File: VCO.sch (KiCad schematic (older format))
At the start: 76 parts, among them J1 Conn_01x05_Male, J10 FM, J12 PW, J13 saw, J14 sq, J3 V/oct, J4 Conn_01x05_Male, J5 Conn_01x05_Male, J6 Conn_01x05_Male, J8 Conn_01x05_Male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

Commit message: Edeting .gitignore
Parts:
- C10, C7, C8, C9: value 1u -> C
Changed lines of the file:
@@
 $EndComp
 $Comp
-L uRack:-9V #PWR0105
+L power:-9V #PWR0105
 U 1 1 5FD658D4
 P 1550 6500
@@
 $EndComp
 $Comp
-L uRack:+9V #PWR0106
+L power:+9V #PWR0106
 U 1 1 5FD84C6F
 P 1650 5200
@@
 P 2950 5500
 F 0 "C9" H 3065 5546 50  0000 L CNN
-F 1 "1u" H 3065 5455 50  0000 L CNN
+F 1 "C" H 3065 5455 50  0000 L CNN
 F 2 "Capacitor_SMD:C_0603_1608Metric_Pad1.05x0.95mm_HandSolder" H 2988 5350 50  0001 C CNN
 F 3 "~" H 2950 5500 50  0001 C CNN
@@
 P 2950 6200
 F 0 "C10" H 3065 6246 50  0000 L CNN
-F 1 "1u" H 3065 6155 50  0000 L CNN
+F 1 "C" H 3065 6155 50  0000 L CNN
 F 2 "Capacitor_SMD:C_0603_1608Metric_Pad1.05x0.95mm_HandSolder" H 2988 6050 50  0001 C CNN
 F 3 "~" H 2950 6200 50  0001 C CNN
@@
 P 1750 5550
 F 0 "C7" H 1865 5596 50  0000 L CNN
-F 1 "1u" H 1865 5505 50  0000 L CNN
+F 1 "C" H 1865 5505 50  0000 L CNN
 F 2 "Capacitor_SMD:C_0603_1608Metric_Pad1.05x0.95mm_HandSolder" H 1788 5400 50  0001 C CNN
 F 3 "~" H 1750 5550 50  0001 C CNN
@@
 P 1750 6150
 F 0 "C8" H 1865 6196 50  0000 L CNN
-F 1 "1u" H 1865 6105 50  0000 L CNN
+F 1 "C" H 1865 6105 50  0000 L CNN
 F 2 "Capacitor_SMD:C_0603_1608Metric_Pad1.05x0.95mm_HandSolder" H 1788 6000 50  0001 C CNN
 F 3 "~" H 1750 6150 50  0001 C CNN
@@
 $EndComp
 $Comp
-L uRack:GNDREF #PWR0109
+L uRack:GNDREF #PWR?
 U 1 1 5FA50368
 P 2200 2000
-F 0 "#PWR0109" H 2200 1750 50  0001 C CNN
+F 0 "#PWR?" H 2200 1750 50  0001 C CNN
 F 1 "GNDREF" H 2205 1827 50  0000 C CNN
 F 2 "" H 2200 2000 50  0001 C CNN
@@
 $EndComp
 $Comp
-L uRack:GNDREF #PWR0110
+L uRack:GNDREF #PWR?
 U 1 1 5FA5270D
 P 2500 2000
-F 0 "#PWR0110" H 2500 1750 50  0001 C CNN
+F 0 "#PWR?" H 2500 1750 50  0001 C CNN
 F 1 "GNDREF" H 2505 1827 50  0000 C CNN
 F 2 "" H 2500 2000 50  0001 C CNN
@@
 $EndComp
 $Comp
-L uRack:GNDREF #PWR0111
+L uRack:GNDREF #PWR?
 U 1 1 5FA67393
 P 2800 2000
-F 0 "#PWR0111" H 2800 1750 50  0001 C CNN
+F 0 "#PWR?" H 2800 1750 50  0001 C CNN
 F 1 "GNDREF" H 2805 1827 50  0000 C CNN
 F 2 "" H 2800 2000 50  0001 C CNN
@@
 $EndComp
 $Comp
-L uRack:GNDREF #PWR0112
+L uRack:GNDREF #PWR?
 U 1 1 5FA7CC97
 P 3700 1850
-F 0 "#PWR0112" H 3700 1600 50  0001 C CNN
+F 0 "#PWR?" H 3700 1600 50  0001 C CNN
 F 1 "GNDREF" H 3705 1677 50  0000 C CNN
 F 2 "" H 3700 1850 50  0001 C CNN
@@
 $EndComp
 $Comp
-L uRack:GNDREF #PWR0113
+L uRack:GNDREF #PWR?
 U 1 1 5FA921D0
 P 4850 3300
-F 0 "#PWR0113" H 4850 3050 50  0001 C CNN
+F 0 "#PWR?" H 4850 3050 50  0001 C CNN
 F 1 "GNDREF" H 4855 3127 50  0000 C CNN
 F 2 "" H 4850 3300 50  0001 C CNN
@@
 $EndComp
 $Comp
-L uRack:GNDREF #PWR0114
+L uRack:GNDREF #PWR?
 U 1 1 5FAA9013
 P 1750 4250
-F 0 "#PWR0114" H 1750 4000 50  0001 C CNN
+F 0 "#PWR?" H 1750 4000 50  0001 C CNN
 F 1 "GNDREF" H 1755 4077 50  0000 C CNN
 F 2 "" H 1750 4250 50  0001 C CNN
@@
 $EndComp
 $Comp
-L uRack:GNDREF #PWR0115
+L uRack:GNDREF #PWR?
 U 1 1 5FABFCE4
 P 2050 4250
-F 0 "#PWR0115" H 2050 4000 50  0001 C CNN
+F 0 "#PWR?" H 2050 4000 50  0001 C CNN
 F 1 "GNDREF" H 2055 4077 50  0000 C CNN
 F 2 "" H 2050 4250 50  0001 C CNN
@@
 $EndComp
 $Comp
-L uRack:GNDREF #PWR0116
+L uRack:GNDREF #PWR?
 U 1 1 5FAD4ADE
 P 2350 4250
-F 0 "#PWR0116" H 2350 4000 50  0001 C CNN
+F 0 "#PWR?" H 2350 4000 50  0001 C CNN
 F 1 "GNDREF" H 2355 4077 50  0000 C CNN
 F 2 "" H 2350 4250 50  0001 C CNN
@@
 $EndComp
 $Comp
-L uRack:GNDREF #PWR0117
+L uRack:GNDREF #PWR?
 U 1 1 5FAE9A25
 P 3300 3950
-F 0 "#PWR0117" H 3300 3700 50  0001 C CNN
+F 0 "#PWR?" H 3300 3700 50  0001 C CNN
 F 1 "GNDREF" H 3305 3777 50  0000 C CNN
 F 2 "" H 3300 3950 50  0001 C CNN
@@
 $EndComp
 $Comp
-L uRack:GNDREF #PWR0118
+L uRack:GNDREF #PWR?
 U 1 1 5FB00E11
 P 3350 5850
-F 0 "#PWR0118" H 3350 5600 50  0001 C CNN
+F 0 "#PWR?" H 3350 5600 50  0001 C CNN
 F 1 "GNDREF" H 3355 5677 50  0000 C CNN
 F 2 "" H 3350 5850 50  0001 C CNN
@@
 $EndComp
 $Comp
-L uRack:GNDREF #PWR0119
+L uRack:GNDREF #PWR?
 U 1 1 5FB17C73
 P 5150 6000
-F 0 "#PWR0119" H 5150 5750 50  0001 C CNN
+F 0 "#PWR?" H 5150 5750 50  0001 C CNN
 F 1 "GNDREF" H 5155 5827 50  0000 C CNN
 F 2 "" H 5150 6000 50  0001 C CNN
@@
 $EndComp
 $Comp
-L uRack:GNDREF #PWR0120
+L uRack:GNDREF #PWR?
 U 1 1 5FB2CB7A
 P 5450 6000
-F 0 "#PWR0120" H 5450 5750 50  0001 C CNN
+F 0 "#PWR?" H 5450 5750 50  0001 C CNN
 F 1 "GNDREF" H 5455 5827 50  0000 C CNN
 F 2 "" H 5450 6000 50  0001 C CNN
@@
 $EndComp
 $Comp
-L uRack:GNDREF #PWR0121
+L uRack:GNDREF #PWR?
 U 1 1 5FB41AD2
 P 5750 6000
-F 0 "#PWR0121" H 5750 5750 50  0001 C CNN
+F 0 "#PWR?" H 5750 5750 50  0001 C CNN
 F 1 "GNDREF" H 5755 5827 50  0000 C CNN
 F 2 "" H 5750 6000 50  0001 C CNN
@@
 $EndComp
 $Comp
-L uRack:GNDREF #PWR0122
+L uRack:GNDREF #PWR?
 U 1 1 5FB56D95
 P 5100 6650
-F 0 "#PWR0122" H 5100 6400 50  0001 C CNN
+F 0 "#PWR?" H 5100 6400 50  0001 C CNN
 F 1 "GNDREF" H 5105 6477 50  0000 C CNN
 F 2 "" H 5100 6650 50  0001 C CNN
@@
 $EndComp
 $Comp
-L uRack:GNDREF #PWR0123
+L uRack:GNDREF #PWR?
 U 1 1 5FB6BB62
 P 5550 6650
-F 0 "#PWR0123" H 5550 6400 50  0001 C CNN
+F 0 "#PWR?" H 5550 6400 50  0001 C CNN
 F 1 "GNDREF" H 5555 6477 50  0000 C CNN
 F 2 "" H 5550 6650 50  0001 C CNN
@@
 $EndComp
 $Comp
-L uRack:GNDREF #PWR0124
+L uRack:GNDREF #PWR?
 U 1 1 5FB8114C
 P 5100 7550
-F 0 "#PWR0124" H 5100 7300 50  0001 C CNN
+F 0 "#PWR?" H 5100 7300 50  0001 C CNN
 F 1 "GNDREF" H 5105 7377 50  0000 C CNN
 F 2 "" H 5100 7550 50  0001 C CNN
@@
 $EndComp
 $Comp
-L uRack:GNDREF #PWR0125
+L uRack:GNDREF #PWR?
 U 1 1 5FB9600F
 P 5550 7550
-F 0 "#PWR0125" H 5550 7300 50  0001 C CNN
+F 0 "#PWR?" H 5550 7300 50  0001 C CNN
 F 1 "GNDREF" H 5555 7377 50  0000 C CNN
 F 2 "" H 5550 7550 50  0001 C CNN
@@
 $EndComp
 $Comp
-L uRack:GNDREF #PWR0126
+L uRack:GNDREF #PWR?
 U 1 1 5FBACAE5
 P 6350 5000
-F 0 "#PWR0126" H 6350 4750 50  0001 C CNN
+F 0 "#PWR?" H 6350 4750 50  0001 C CNN
 F 1 "GNDREF" H 6355 4827 50  0000 C CNN
 F 2 "" H 6350 5000 50  0001 C CNN
@@
 $EndComp
 $Comp
-L uRack:GNDREF #PWR0127
+L uRack:GNDREF #PWR?
 U 1 1 5FBC2590
 P 8500 5200
-F 0 "#PWR0127" H 8500 4950 50  0001 C CNN
+F 0 "#PWR?" H 8500 4950 50  0001 C CNN
 F 1 "GNDREF" H 8505 5027 50  0000 C CNN
 F 2 "" H 8500 5200 50  0001 C CNN
@@
 $EndComp
 $Comp
-L uRack:GNDREF #PWR0128
+L uRack:GNDREF #PWR?
 U 1 1 5FBD8A79
 P 7350 4150
-F 0 "#PWR0128" H 7350 3900 50  0001 C CNN
+F 0 "#PWR?" H 7350 3900 50  0001 C CNN
 F 1 "GNDREF" H 7355 3977 50  0000 C CNN
 F 2 "" H 7350 4150 50  0001 C CNN
@@
 $EndComp
 $Comp
-L uRack:GNDREF #PWR0129
+L uRack:GNDREF #PWR?
 U 1 1 5FBF0885
 P 7100 2950
-F 0 "#PWR0129" H 7100 2700 50  0001 C CNN
+F 0 "#PWR?" H 7100 2700 50  0001 C CNN
 F 1 "GNDREF" H 7105 2777 50  0000 C CNN
 F 2 "" H 7100 2950 50  0001 C CNN
@@
 $EndComp
 $Comp
-L uRack:GNDREF #PWR0130
+L uRack:GNDREF #PWR?
 U 1 1 5FC05D36
 P 8600 3700
-F 0 "#PWR0130" H 8600 3450 50  0001 C CNN
+F 0 "#PWR?" H 8600 3450 50  0001 C CNN
 F 1 "GNDREF" H 8605 3527 50  0000 C CNN
 F 2 "" H 8600 3700 50  0001 C CNN
@@
 $EndComp
 $Comp
-L uRack:GNDREF #PWR0131
+L uRack:GNDREF #PWR?
 U 1 1 5FC1CEB4
 P 10200 2900
-F 0 "#PWR0131" H 10200 2650 50  0001 C CNN
+F 0 "#PWR?" H 10200 2650 50  0001 C CNN
 F 1 "GNDREF" H 10205 2727 50  0000 C CNN
 F 2 "" H 10200 2900 50  0001 C CNN
@@
 $EndComp
 $Comp
-L uRack:GNDREF #PWR0132
+L uRack:GNDREF #PWR?
 U 1 1 5FC3297A
 P 7000 1800
-F 0 "#PWR0132" H 7000 1550 50  0001 C CNN
+F 0 "#PWR?" H 7000 1550 50  0001 C CNN
 F 1 "GNDREF" H 7005 1627 50  0000 C CNN
 F 2 "" H 7000 1800 50  0001 C CNN
@@
 $EndComp
 $Comp
-L uRack:GNDREF #PWR0133
+L uRack:GNDREF #PWR?
 U 1 1 5FC493B8
 P 6550 1650
-F 0 "#PWR0133" H 6550 1400 50  0001 C CNN
+F 0 "#PWR?" H 6550 1400 50  0001 C CNN
 F 1 "GNDREF" H 6555 1477 50  0000 C CNN
 F 2 "" H 6550 1650 50  0001 C CNN

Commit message: use power symbols from urack library, specify LDO caps
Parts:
- C10, C7, C8, C9: value C -> 1u
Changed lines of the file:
@@
 $EndComp
 $Comp
-L power:-9V #PWR0105
+L uRack:-9V #PWR0105
 U 1 1 5FD658D4
 P 1550 6500
@@
 $EndComp
 $Comp
-L power:+9V #PWR0106
+L uRack:+9V #PWR0106
 U 1 1 5FD84C6F
 P 1650 5200
@@
 P 2950 5500
 F 0 "C9" H 3065 5546 50  0000 L CNN
-F 1 "C" H 3065 5455 50  0000 L CNN
+F 1 "1u" H 3065 5455 50  0000 L CNN
 F 2 "Capacitor_SMD:C_0603_1608Metric_Pad1.05x0.95mm_HandSolder" H 2988 5350 50  0001 C CNN
 F 3 "~" H 2950 5500 50  0001 C CNN
@@
 P 2950 6200
 F 0 "C10" H 3065 6246 50  0000 L CNN
-F 1 "C" H 3065 6155 50  0000 L CNN
+F 1 "1u" H 3065 6155 50  0000 L CNN
 F 2 "Capacitor_SMD:C_0603_1608Metric_Pad1.05x0.95mm_HandSolder" H 2988 6050 50  0001 C CNN
 F 3 "~" H 2950 6200 50  0001 C CNN
@@
 P 1750 5550
 F 0 "C7" H 1865 5596 50  0000 L CNN
-F 1 "C" H 1865 5505 50  0000 L CNN
+F 1 "1u" H 1865 5505 50  0000 L CNN
 F 2 "Capacitor_SMD:C_0603_1608Metric_Pad1.05x0.95mm_HandSolder" H 1788 5400 50  0001 C CNN
 F 3 "~" H 1750 5550 50  0001 C CNN
@@
 P 1750 6150
 F 0 "C8" H 1865 6196 50  0000 L CNN
-F 1 "C" H 1865 6105 50  0000 L CNN
+F 1 "1u" H 1865 6105 50  0000 L CNN
 F 2 "Capacitor_SMD:C_0603_1608Metric_Pad1.05x0.95mm_HandSolder" H 1788 6000 50  0001 C CNN
 F 3 "~" H 1750 6150 50  0001 C CNN
@@
 $EndComp
 $Comp
-L uRack:GNDREF #PWR?
+L uRack:GNDREF #PWR0109
 U 1 1 5FA50368
 P 2200 2000
-F 0 "#PWR?" H 2200 1750 50  0001 C CNN
+F 0 "#PWR0109" H 2200 1750 50  0001 C CNN
 F 1 "GNDREF" H 2205 1827 50  0000 C CNN
 F 2 "" H 2200 2000 50  0001 C CNN
@@
 $EndComp
 $Comp
-L uRack:GNDREF #PWR?
+L uRack:GNDREF #PWR0110
 U 1 1 5FA5270D
 P 2500 2000
-F 0 "#PWR?" H 2500 1750 50  0001 C CNN
+F 0 "#PWR0110" H 2500 1750 50  0001 C CNN
 F 1 "GNDREF" H 2505 1827 50  0000 C CNN
 F 2 "" H 2500 2000 50  0001 C CNN
@@
 $EndComp
 $Comp
-L uRack:GNDREF #PWR?
+L uRack:GNDREF #PWR0111
 U 1 1 5FA67393
 P 2800 2000
-F 0 "#PWR?" H 2800 1750 50  0001 C CNN
+F 0 "#PWR0111" H 2800 1750 50  0001 C CNN
 F 1 "GNDREF" H 2805 1827 50  0000 C CNN
 F 2 "" H 2800 2000 50  0001 C CNN
@@
 $EndComp
 $Comp
-L uRack:GNDREF #PWR?
+L uRack:GNDREF #PWR0112
 U 1 1 5FA7CC97
 P 3700 1850
-F 0 "#PWR?" H 3700 1600 50  0001 C CNN
+F 0 "#PWR0112" H 3700 1600 50  0001 C CNN
 F 1 "GNDREF" H 3705 1677 50  0000 C CNN
 F 2 "" H 3700 1850 50  0001 C CNN
@@
 $EndComp
 $Comp
-L uRack:GNDREF #PWR?
+L uRack:GNDREF #PWR0113
 U 1 1 5FA921D0
 P 4850 3300
-F 0 "#PWR?" H 4850 3050 50  0001 C CNN
+F 0 "#PWR0113" H 4850 3050 50  0001 C CNN
 F 1 "GNDREF" H 4855 3127 50  0000 C CNN
 F 2 "" H 4850 3300 50  0001 C CNN
@@
 $EndComp
 $Comp
-L uRack:GNDREF #PWR?
+L uRack:GNDREF #PWR0114
 U 1 1 5FAA9013
 P 1750 4250
-F 0 "#PWR?" H 1750 4000 50  0001 C CNN
+F 0 "#PWR0114" H 1750 4000 50  0001 C CNN
 F 1 "GNDREF" H 1755 4077 50  0000 C CNN
 F 2 "" H 1750 4250 50  0001 C CNN
@@
 $EndComp
 $Comp
-L uRack:GNDREF #PWR?
+L uRack:GNDREF #PWR0115
 U 1 1 5FABFCE4
 P 2050 4250
-F 0 "#PWR?" H 2050 4000 50  0001 C CNN
+F 0 "#PWR0115" H 2050 4000 50  0001 C CNN
 F 1 "GNDREF" H 2055 4077 50  0000 C CNN
 F 2 "" H 2050 4250 50  0001 C CNN
@@
 $EndComp
 $Comp
-L uRack:GNDREF #PWR?
+L uRack:GNDREF #PWR0116
 U 1 1 5FAD4ADE
 P 2350 4250
-F 0 "#PWR?" H 2350 4000 50  0001 C CNN
+F 0 "#PWR0116" H 2350 4000 50  0001 C CNN
 F 1 "GNDREF" H 2355 4077 50  0000 C CNN
 F 2 "" H 2350 4250 50  0001 C CNN
@@
 $EndComp
 $Comp
-L uRack:GNDREF #PWR?
+L uRack:GNDREF #PWR0117
 U 1 1 5FAE9A25
 P 3300 3950
-F 0 "#PWR?" H 3300 3700 50  0001 C CNN
+F 0 "#PWR0117" H 3300 3700 50  0001 C CNN
 F 1 "GNDREF" H 3305 3777 50  0000 C CNN
 F 2 "" H 3300 3950 50  0001 C CNN
@@
 $EndComp
 $Comp
-L uRack:GNDREF #PWR?
+L uRack:GNDREF #PWR0118
 U 1 1 5FB00E11
 P 3350 5850
-F 0 "#PWR?" H 3350 5600 50  0001 C CNN
+F 0 "#PWR0118" H 3350 5600 50  0001 C CNN
 F 1 "GNDREF" H 3355 5677 50  0000 C CNN
 F 2 "" H 3350 5850 50  0001 C CNN
@@
 $EndComp
 $Comp
-L uRack:GNDREF #PWR?
+L uRack:GNDREF #PWR0119
 U 1 1 5FB17C73
 P 5150 6000
-F 0 "#PWR?" H 5150 5750 50  0001 C CNN
+F 0 "#PWR0119" H 5150 5750 50  0001 C CNN
 F 1 "GNDREF" H 5155 5827 50  0000 C CNN
 F 2 "" H 5150 6000 50  0001 C CNN
@@
 $EndComp
 $Comp
-L uRack:GNDREF #PWR?
+L uRack:GNDREF #PWR0120
 U 1 1 5FB2CB7A
 P 5450 6000
-F 0 "#PWR?" H 5450 5750 50  0001 C CNN
+F 0 "#PWR0120" H 5450 5750 50  0001 C CNN
 F 1 "GNDREF" H 5455 5827 50  0000 C CNN
 F 2 "" H 5450 6000 50  0001 C CNN
@@
 $EndComp
 $Comp
-L uRack:GNDREF #PWR?
+L uRack:GNDREF #PWR0121
 U 1 1 5FB41AD2
 P 5750 6000
-F 0 "#PWR?" H 5750 5750 50  0001 C CNN
+F 0 "#PWR0121" H 5750 5750 50  0001 C CNN
 F 1 "GNDREF" H 5755 5827 50  0000 C CNN
 F 2 "" H 5750 6000 50  0001 C CNN
@@
 $EndComp
 $Comp
-L uRack:GNDREF #PWR?
+L uRack:GNDREF #PWR0122
 U 1 1 5FB56D95
 P 5100 6650
-F 0 "#PWR?" H 5100 6400 50  0001 C CNN
+F 0 "#PWR0122" H 5100 6400 50  0001 C CNN
 F 1 "GNDREF" H 5105 6477 50  0000 C CNN
 F 2 "" H 5100 6650 50  0001 C CNN
@@
 $EndComp
 $Comp
-L uRack:GNDREF #PWR?
+L uRack:GNDREF #PWR0123
 U 1 1 5FB6BB62
 P 5550 6650
-F 0 "#PWR?" H 5550 6400 50  0001 C CNN
+F 0 "#PWR0123" H 5550 6400 50  0001 C CNN
 F 1 "GNDREF" H 5555 6477 50  0000 C CNN
 F 2 "" H 5550 6650 50  0001 C CNN
@@
 $EndComp
 $Comp
-L uRack:GNDREF #PWR?
+L uRack:GNDREF #PWR0124
 U 1 1 5FB8114C
 P 5100 7550
-F 0 "#PWR?" H 5100 7300 50  0001 C CNN
+F 0 "#PWR0124" H 5100 7300 50  0001 C CNN
 F 1 "GNDREF" H 5105 7377 50  0000 C CNN
 F 2 "" H 5100 7550 50  0001 C CNN
@@
 $EndComp
 $Comp
-L uRack:GNDREF #PWR?
+L uRack:GNDREF #PWR0125
 U 1 1 5FB9600F
 P 5550 7550
-F 0 "#PWR?" H 5550 7300 50  0001 C CNN
+F 0 "#PWR0125" H 5550 7300 50  0001 C CNN
 F 1 "GNDREF" H 5555 7377 50  0000 C CNN
 F 2 "" H 5550 7550 50  0001 C CNN
@@
 $EndComp
 $Comp
-L uRack:GNDREF #PWR?
+L uRack:GNDREF #PWR0126
 U 1 1 5FBACAE5
 P 6350 5000
-F 0 "#PWR?" H 6350 4750 50  0001 C CNN
+F 0 "#PWR0126" H 6350 4750 50  0001 C CNN
 F 1 "GNDREF" H 6355 4827 50  0000 C CNN
 F 2 "" H 6350 5000 50  0001 C CNN
@@
 $EndComp
 $Comp
-L uRack:GNDREF #PWR?
+L uRack:GNDREF #PWR0127
 U 1 1 5FBC2590
 P 8500 5200
-F 0 "#PWR?" H 8500 4950 50  0001 C CNN
+F 0 "#PWR0127" H 8500 4950 50  0001 C CNN
 F 1 "GNDREF" H 8505 5027 50  0000 C CNN
 F 2 "" H 8500 5200 50  0001 C CNN
@@
 $EndComp
 $Comp
-L uRack:GNDREF #PWR?
+L uRack:GNDREF #PWR0128
 U 1 1 5FBD8A79
 P 7350 4150
-F 0 "#PWR?" H 7350 3900 50  0001 C CNN
+F 0 "#PWR0128" H 7350 3900 50  0001 C CNN
 F 1 "GNDREF" H 7355 3977 50  0000 C CNN
 F 2 "" H 7350 4150 50  0001 C CNN
@@
 $EndComp
 $Comp
-L uRack:GNDREF #PWR?
+L uRack:GNDREF #PWR0129
 U 1 1 5FBF0885
 P 7100 2950
-F 0 "#PWR?" H 7100 2700 50  0001 C CNN
+F 0 "#PWR0129" H 7100 2700 50  0001 C CNN
 F 1 "GNDREF" H 7105 2777 50  0000 C CNN
 F 2 "" H 7100 2950 50  0001 C CNN
@@
 $EndComp
 $Comp
-L uRack:GNDREF #PWR?
+L uRack:GNDREF #PWR0130
 U 1 1 5FC05D36
 P 8600 3700
-F 0 "#PWR?" H 8600 3450 50  0001 C CNN
+F 0 "#PWR0130" H 8600 3450 50  0001 C CNN
 F 1 "GNDREF" H 8605 3527 50  0000 C CNN
 F 2 "" H 8600 3700 50  0001 C CNN
@@
 $EndComp
 $Comp
-L uRack:GNDREF #PWR?
+L uRack:GNDREF #PWR0131
 U 1 1 5FC1CEB4
 P 10200 2900
-F 0 "#PWR?" H 10200 2650 50  0001 C CNN
+F 0 "#PWR0131" H 10200 2650 50  0001 C CNN
 F 1 "GNDREF" H 10205 2727 50  0000 C CNN
 F 2 "" H 10200 2900 50  0001 C CNN
@@
 $EndComp
 $Comp
-L uRack:GNDREF #PWR?
+L uRack:GNDREF #PWR0132
 U 1 1 5FC3297A
 P 7000 1800
-F 0 "#PWR?" H 7000 1550 50  0001 C CNN
+F 0 "#PWR0132" H 7000 1550 50  0001 C CNN
 F 1 "GNDREF" H 7005 1627 50  0000 C CNN
 F 2 "" H 7000 1800 50  0001 C CNN
@@
 $EndComp
 $Comp
-L uRack:GNDREF #PWR?
+L uRack:GNDREF #PWR0133
 U 1 1 5FC493B8
 P 6550 1650
-F 0 "#PWR?" H 6550 1400 50  0001 C CNN
+F 0 "#PWR0133" H 6550 1400 50  0001 C CNN
 F 1 "GNDREF" H 6555 1477 50  0000 C CNN
 F 2 "" H 6550 1650 50  0001 C CNN

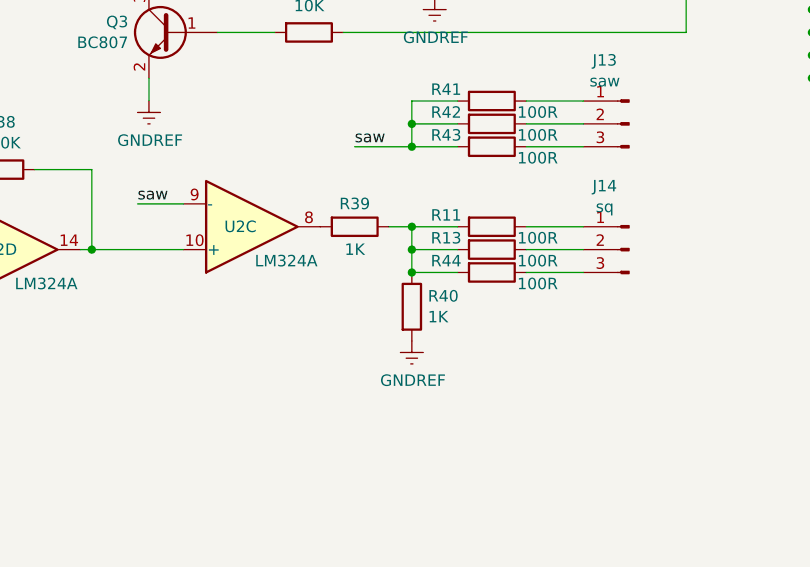
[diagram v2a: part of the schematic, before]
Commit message: change square-wave output divider
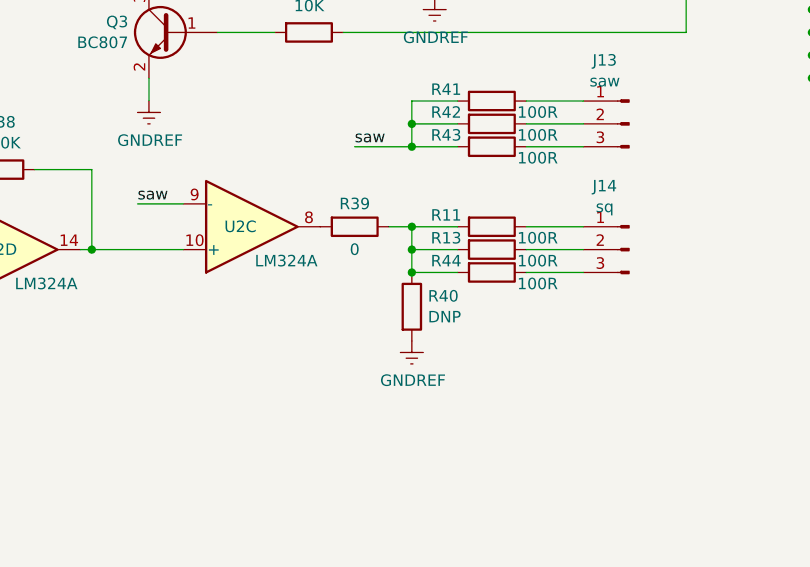
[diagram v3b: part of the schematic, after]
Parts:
- R39: value 1K -> 0
- R40: value 1K -> DNP
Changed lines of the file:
@@
 P 8250 4700
 F 0 "R39" V 8150 4700 50  0000 C CNN
-F 1 "1K" V 8350 4700 50  0000 C CNN
+F 1 "0" V 8350 4700 50  0000 C CNN
 F 2 "footprint:r0603" V 8180 4700 50  0001 C CNN
 F 3 "~" H 8250 4700 50  0001 C CNN
@@
 P 8500 5050
 F 0 "R40" H 8570 5096 50  0000 L CNN
-F 1 "1K" H 8570 5005 50  0000 L CNN
+F 1 "DNP" H 8570 5005 50  0000 L CNN
 F 2 "footprint:r0603" V 8430 5050 50  0001 C CNN
 F 3 "~" H 8500 5050 50  0001 C CNN
